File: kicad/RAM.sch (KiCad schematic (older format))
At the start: 8 parts, among them U105 74LS08, U106 74LS08, U107 74LS08, U108 74LS04, U109 74LS04, U110 628128_DIP32_SSOP32, U111 28C256, U112 74LS245

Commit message: Finish todo list
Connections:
- net RAM_2: no longer U112.2 (A0)
- net RAM_3: no longer U112.3 (A1)
- net RAM_4: no longer U112.4 (A2)
- net RAM_5: no longer U112.5 (A3)
- net RAM_6: no longer U112.6 (A4)
- net RAM_7: no longer U112.7 (A5)
- net RAM_8: no longer U112.8 (A6)
- net RAM_9: no longer U112.9 (A7)
- new net RAMO_0: U112.9 (A7)
- new net RAMO_1: U112.8 (A6)
- new net RAMO_2: U112.7 (A5)
- new net RAMO_3: U112.6 (A4)
- new net RAMO_4: U112.5 (A3)
- new net RAMO_5: U112.4 (A2)
- new net RAMO_6: U112.3 (A1)
- new net RAMO_7: U112.2 (A0)
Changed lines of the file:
@@
 Sheet 16 26
 Title ""
-Date "2019-09-26"
+Date "2019-10-03"
 Rev "v0.1"
 Comp "Christopher Milan"
@@
 Wire Wire Line
 	1550 2500 3400 2500
-Wire Wire Line
-	3400 2600 2900 2600
-Wire Wire Line
-	1550 2700 2950 2700
 Wire Wire Line
 	3400 2800 3000 2800
@@
 Wire Wire Line
 	7000 2850 6550 2850
-Connection ~ 2950 2700
-Wire Wire Line
-	2950 2700 3400 2700
 Wire Wire Line
 	6500 2750 7000 2750
-Connection ~ 2900 2600
-Wire Wire Line
-	2900 2600 1550 2600
 Wire Wire Line
 	6500 1950 7000 1950
@@
 	3350 3500 3350 3800
 Wire Wire Line
-	2900 2600 2900 4250
-Wire Wire Line
-	2950 4200 2950 2700
-Wire Wire Line
 	3000 4150 3000 2800
 Wire Wire Line
@@
 	4850 5800 4850 5750
 Wire Wire Line
-	5150 5750 5150 6050
-Wire Wire Line
-	5150 6050 2900 6050
-Wire Wire Line
-	2900 6050 2900 4250
-Connection ~ 2900 4250
-Wire Wire Line
-	2950 4200 2950 6100
-Wire Wire Line
-	2950 6100 5250 6100
-Wire Wire Line
-	5250 6100 5250 5750
-Connection ~ 2950 4200
-Wire Wire Line
-	5350 5750 5350 6150
-Wire Wire Line
-	5350 6150 3000 6150
-Wire Wire Line
-	3000 6150 3000 4150
-Connection ~ 3000 4150
-Wire Wire Line
-	3050 6200 5450 6200
-Wire Wire Line
-	5450 6200 5450 5750
+	5150 5750 5150 5800
+Wire Wire Line
+	5250 5800 5250 5750
+Wire Wire Line
+	5350 5750 5350 5800
+Wire Wire Line
+	5450 5800 5450 5750
 Wire Wire Line
 	3050 2900 3050 4100
-Connection ~ 3050 4100
-Wire Wire Line
-	3050 4100 3050 6200
-Wire Wire Line
-	5550 5750 5550 6250
-Wire Wire Line
-	5550 6250 3100 6250
-Wire Wire Line
-	3100 6250 3100 4050
-Connection ~ 3100 4050
-Wire Wire Line
-	3150 4000 3150 6300
-Wire Wire Line
-	3150 6300 5650 6300
-Wire Wire Line
-	5650 6300 5650 5750
-Connection ~ 3150 4000
-Wire Wire Line
-	5750 5750 5750 6350
-Wire Wire Line
-	5750 6350 3200 6350
-Wire Wire Line
-	3200 6350 3200 3950
-Connection ~ 3200 3950
-Wire Wire Line
-	3250 3900 3250 6400
-Wire Wire Line
-	3250 6400 5850 6400
-Wire Wire Line
-	5850 6400 5850 5750
-Connection ~ 3250 3900
+Wire Wire Line
+	5550 5750 5550 5800
+Wire Wire Line
+	5650 5800 5650 5750
+Wire Wire Line
+	5750 5750 5750 5800
+Wire Wire Line
+	5850 5800 5850 5750
+Wire Wire Line
+	2950 2700 3400 2700
+Wire Wire Line
+	1550 2700 2950 2700
+Connection ~ 2950 2700
+Wire Wire Line
+	2950 4200 2950 2700
+Wire Wire Line
+	2900 2600 1550 2600
+Wire Wire Line
+	3400 2600 2900 2600
+Connection ~ 2900 2600
+Wire Wire Line
+	2900 2600 2900 4250
+Text HLabel 5150 5800 3    50   Output ~ 0
+RAMO_0
+Text HLabel 5250 5800 3    50   Output ~ 0
+RAMO_1
+Text HLabel 5350 5800 3    50   Output ~ 0
+RAMO_2
+Text HLabel 5450 5800 3    50   Output ~ 0
+RAMO_3
+Text HLabel 5550 5800 3    50   Output ~ 0
+RAMO_4
+Text HLabel 5650 5800 3    50   Output ~ 0
+RAMO_5
+Text HLabel 5750 5800 3    50   Output ~ 0
+RAMO_6
+Text HLabel 5850 5800 3    50   Output ~ 0
+RAMO_7
 $EndSCHEMATC

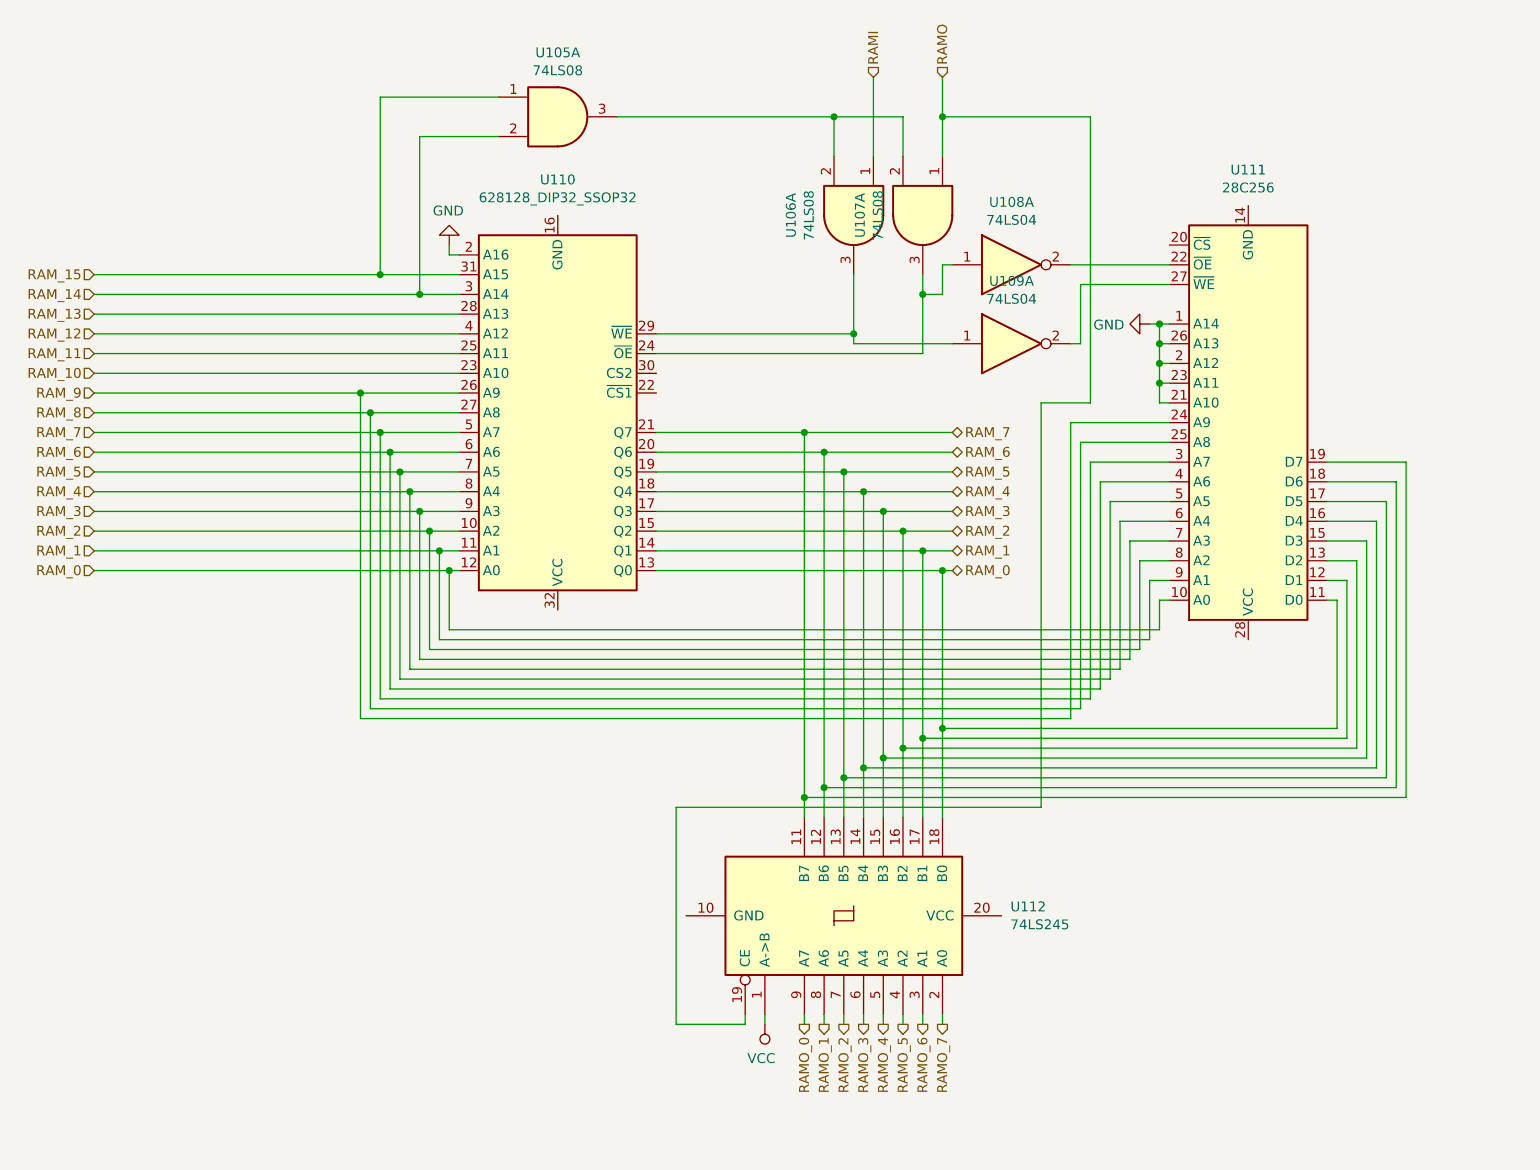
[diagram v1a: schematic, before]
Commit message: Reorganize part references
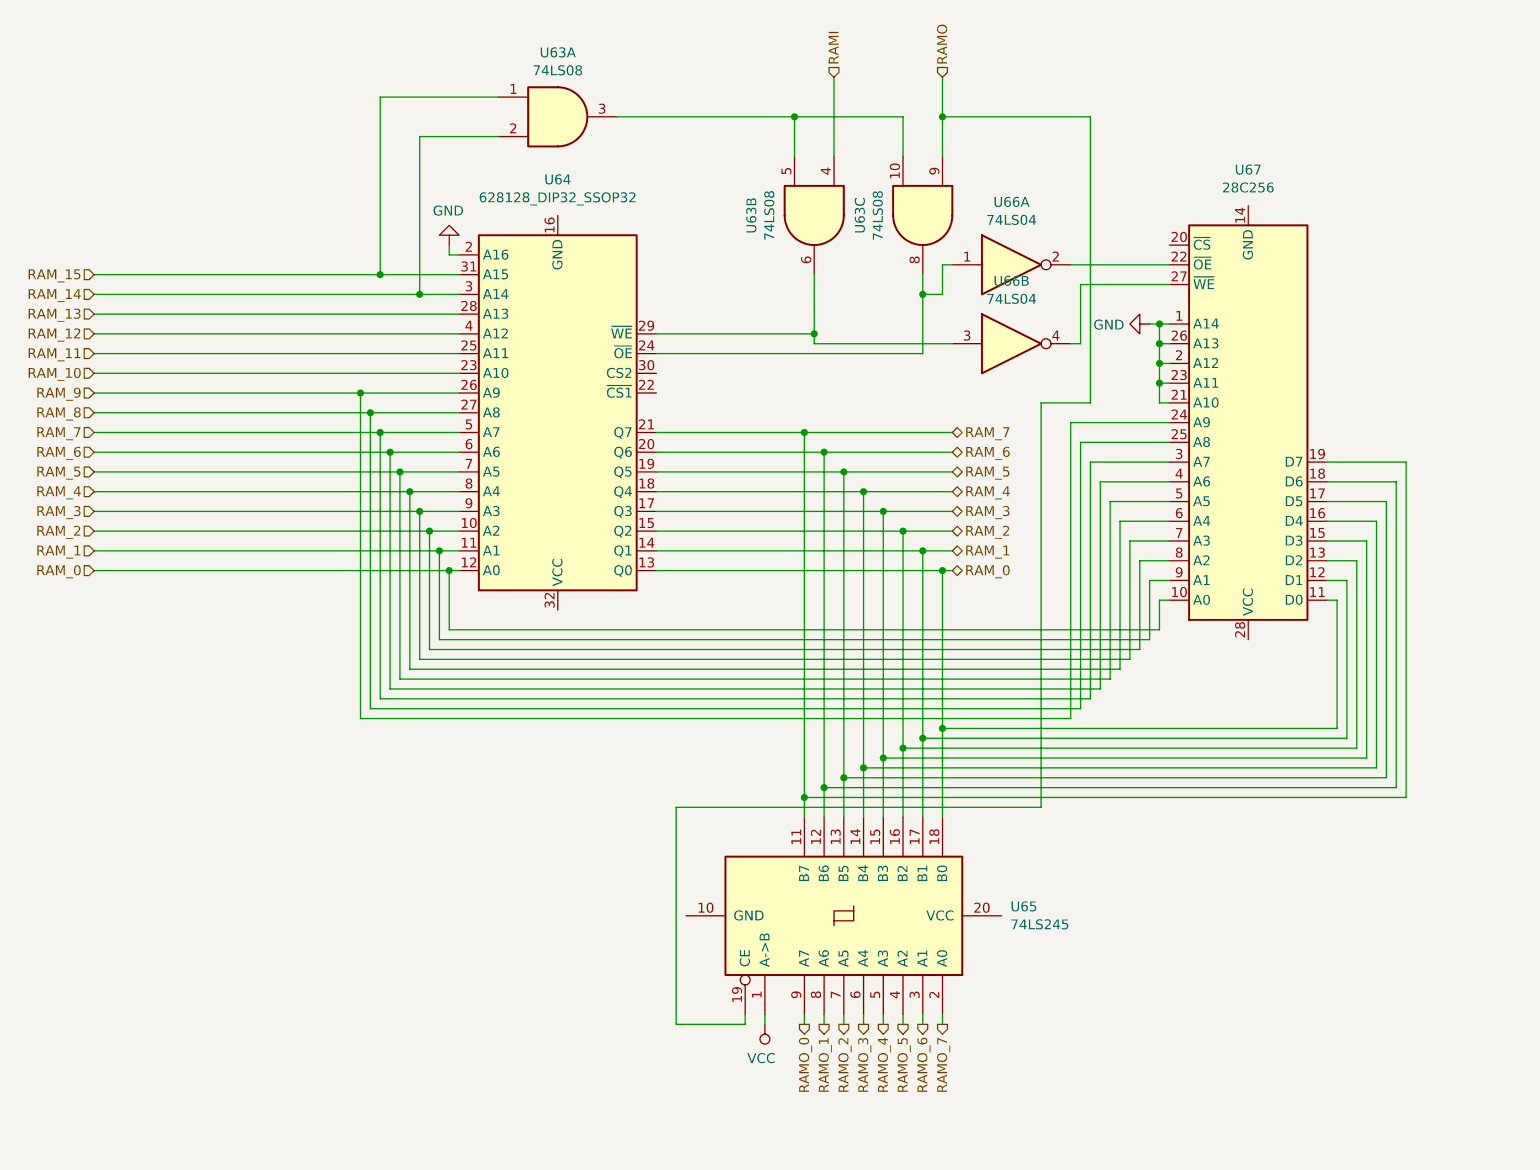
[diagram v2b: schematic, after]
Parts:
- renumbered U106 to U63, U107 to U63, U105 to U63, U110 to U64, U112 to U65, U108 to U66, U109 to U66, U111 to U67
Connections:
- net RAMI: now also U63.4; no longer U63.1
- net RAMO: now also U63.9; no longer U63.1
- net at U64.24 (~OE), U66.1: now also U63.8; no longer U63.3
- net at U67.27 (~WE): now also U66.4; no longer U66.2
- new net: U63.6, U64.29 (~WE), U66.3
- new net: U63.10, U63.3, U63.5
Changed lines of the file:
@@
 P 3900 2700
 AR Path="/5E5B2276/5D858701" Ref="U?"  Part="1"
-AR Path="/5E5B2276/5D857448/5D858701" Ref="U110"  Part="1"
-F 0 "U110" H 3900 1519 50  0000 C CNN
+AR Path="/5E5B2276/5D857448/5D858701" Ref="U64"  Part="1"
+F 0 "U64" H 3900 1519 50  0000 C CNN
 F 1 "628128_DIP32_SSOP32" H 3900 1610 50  0000 C CNN
 F 2 "" H 3900 2700 50  0001 C CNN
@@
 RAM_15
 $Comp
-L 74xx:74LS08 U106
-U 1 1 5D86123E
-P 5400 1700
-F 0 "U106" H 5400 1383 50  0000 C CNN
-F 1 "74LS08" H 5400 1474 50  0000 C CNN
-F 2 "" H 5400 1700 50  0001 C CNN
-F 3 "http://www.ti.com/lit/gpn/sn74LS08" H 5400 1700 50  0001 C CNN
-	1    5400 1700
+L 74xx:74LS08 U63
+U 2 1 5D86123E
+P 5200 1700
+F 0 "U63" H 5200 1383 50  0000 C CNN
+F 1 "74LS08" H 5200 1474 50  0000 C CNN
+F 2 "" H 5200 1700 50  0001 C CNN
+F 3 "http://www.ti.com/lit/gpn/sn74LS08" H 5200 1700 50  0001 C CNN
+	2    5200 1700
 	0    1    1    0
 $EndComp
 $Comp
-L 74xx:74LS08 U107
-U 1 1 5D86652B
+L 74xx:74LS08 U63
+U 3 1 5D86652B
 P 5750 1700
-F 0 "U107" H 5750 1383 50  0000 C CNN
+F 0 "U63" H 5750 1383 50  0000 C CNN
 F 1 "74LS08" H 5750 1474 50  0000 C CNN
 F 2 "" H 5750 1700 50  0001 C CNN
 F 3 "http://www.ti.com/lit/gpn/sn74LS08" H 5750 1700 50  0001 C CNN
-	1    5750 1700
+	3    5750 1700
 	0    1    1    0
 $EndComp
@@
 	3200 1300 3200 2100
 Wire Wire Line
-	5300 1200 5300 1400
-Wire Wire Line
-	5300 1200 5650 1200
+	5100 1200 5100 1400
+Wire Wire Line
+	5100 1200 5650 1200
 Wire Wire Line
 	5650 1200 5650 1400
-Text HLabel 5500 1000 1    50   Input ~ 0
+Text HLabel 5300 1000 1    50   Input ~ 0
 RAMI
 Wire Wire Line
-	5500 1000 5500 1400
+	5300 1000 5300 1400
 Text HLabel 5850 1000 1    50   Input ~ 0
 RAMO
@@
 	5850 1000 5850 1200
 $Comp
-L Memory_EEPROM:28C256 U111
+L Memory_EEPROM:28C256 U67
 U 1 1 5D886118
 P 7400 2750
-F 0 "U111" H 7400 1469 50  0000 C CNN
+F 0 "U67" H 7400 1469 50  0000 C CNN
 F 1 "28C256" H 7400 1560 50  0000 C CNN
 F 2 "" H 7400 2750 50  0001 C CNN
@@
 $EndComp
 Wire Wire Line
-	5300 1200 4200 1200
-Connection ~ 5300 1200
-Wire Wire Line
-	4400 2300 5400 2300
+	5100 1200 4200 1200
+Connection ~ 5100 1200
+Wire Wire Line
+	4400 2300 5200 2300
 Wire Wire Line
 	4400 2400 5750 2400
 $Comp
-L 74xx:74LS04 U108
+L 74xx:74LS04 U66
 U 1 1 5D8C76E3
 P 6200 1950
-F 0 "U108" H 6200 2267 50  0000 C CNN
+F 0 "U66" H 6200 2267 50  0000 C CNN
 F 1 "74LS04" H 6200 2176 50  0000 C CNN
 F 2 "" H 6200 1950 50  0001 C CNN
@@
 $EndComp
 $Comp
-L 74xx:74LS04 U109
-U 1 1 5D8CAB5C
+L 74xx:74LS04 U66
+U 2 1 5D8CAB5C
 P 6200 2350
-F 0 "U109" H 6200 2667 50  0000 C CNN
+F 0 "U66" H 6200 2667 50  0000 C CNN
 F 1 "74LS04" H 6200 2576 50  0000 C CNN
 F 2 "" H 6200 2350 50  0001 C CNN
 F 3 "http://www.ti.com/lit/gpn/sn74LS04" H 6200 2350 50  0001 C CNN
-	1    6200 2350
+	2    6200 2350
 	1    0    0    -1
 $EndComp
@@
 	5750 2000 5750 2100
 Wire Wire Line
-	5400 2000 5400 2300
+	5200 2000 5200 2300
 Wire Wire Line
 	5850 2100 5750 2100
@@
 	6500 1950 7000 1950
 Wire Wire Line
-	5900 2350 5400 2350
-Wire Wire Line
-	5400 2350 5400 2300
-Connection ~ 5400 2300
+	5900 2350 5200 2350
+Wire Wire Line
+	5200 2350 5200 2300
+Connection ~ 5200 2300
 Text HLabel 5900 3500 2    50   BiDi ~ 0
 RAM_0
@@
 	6950 3800 6950 3650
 $Comp
-L 74xx:74LS08 U105
+L 74xx:74LS08 U63
 U 1 1 5DB08B15
 P 3900 1200
-F 0 "U105" H 3900 1525 50  0000 C CNN
+F 0 "U63" H 3900 1525 50  0000 C CNN
 F 1 "74LS08" H 3900 1434 50  0000 C CNN
 F 2 "" H 3900 1200 50  0001 C CNN
@@
 $EndComp
 $Comp
-L 74xx:74LS245 U112
+L 74xx:74LS245 U65
 U 1 1 5DB0B306
 P 5350 5250
-F 0 "U112" V 5396 6094 50  0000 L CNN
+F 0 "U65" V 5396 6094 50  0000 L CNN
 F 1 "74LS245" V 5305 6094 50  0000 L CNN
 F 2 "" H 5350 5250 50  0001 C CNN

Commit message: Up to v1.0 and plot
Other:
- moved on the sheet: U63A, U63B, U63C, U64, U65, U66A, U66B, U67
